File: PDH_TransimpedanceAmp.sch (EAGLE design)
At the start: 21 parts, among them U1 LMH6626, X1 UMC, X2 UMC

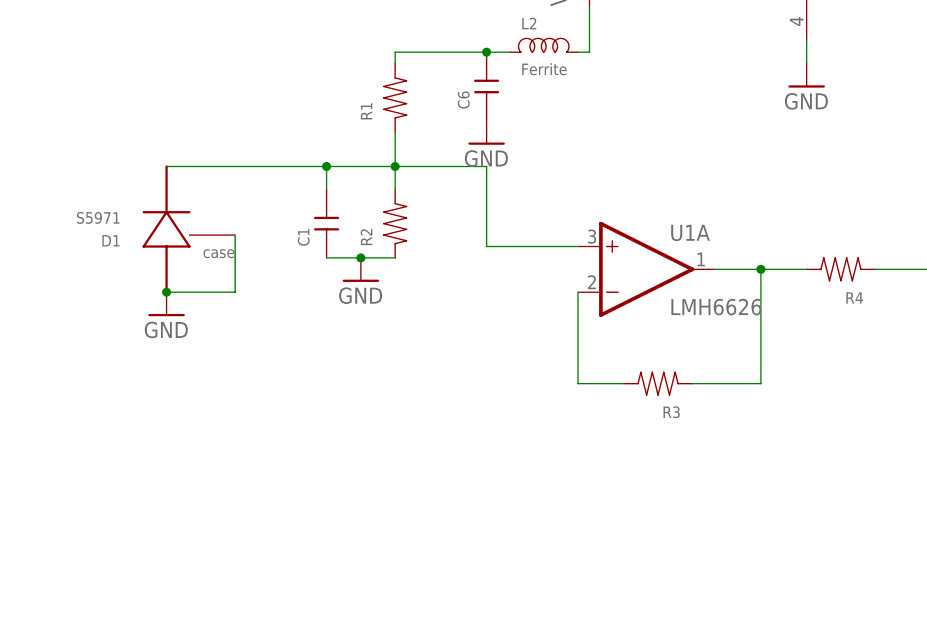
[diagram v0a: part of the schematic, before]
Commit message: Fixed PD net connection; added BW limiting capacitor
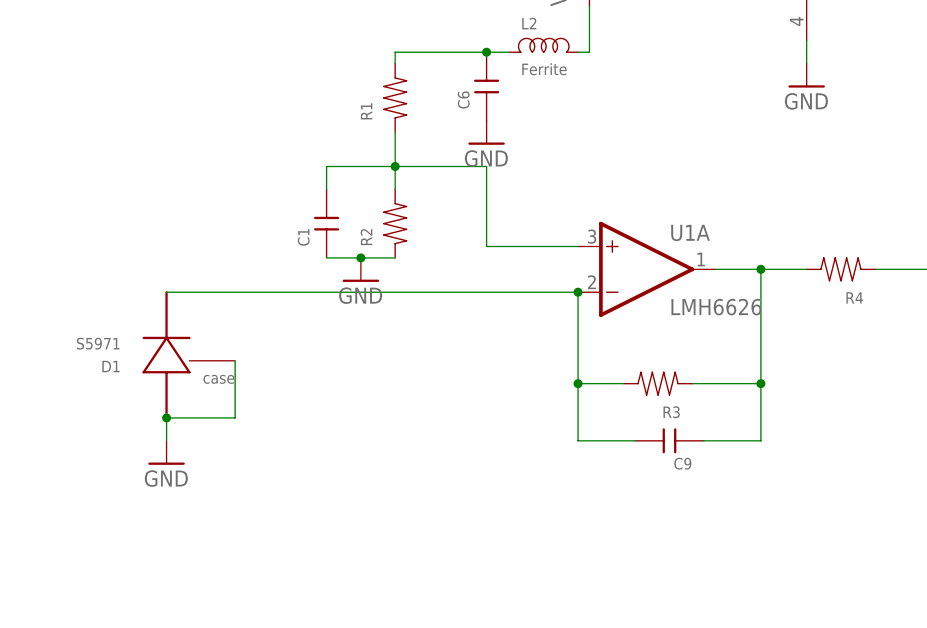
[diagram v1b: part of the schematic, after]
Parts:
- added C9: (no value), rlc-jqi:CAP0402
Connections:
- net N$1: no longer D1.CATHODE
- net N$4: now also C9.P$2, D1.CATHODE
- net N$5: now also C9.P$1
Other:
- moved on the sheet: D1
